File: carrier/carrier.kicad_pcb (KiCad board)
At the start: 2 copper layers, 86.4 x 68.6 mm, 96 parts, among them J1 Conn_01x14, J10 Conn_02x06_Odd_Even, J2 Conn_01x14, J3 Conn_01x14, J4 Conn_01x14, J5 Conn_02x14_Odd_Even, J6 Conn_02x14_Odd_Even, J7 Conn_02x14_Odd_Even, J8 Conn_02x14_Odd_Even, J9 Conn_02x06_Odd_Even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

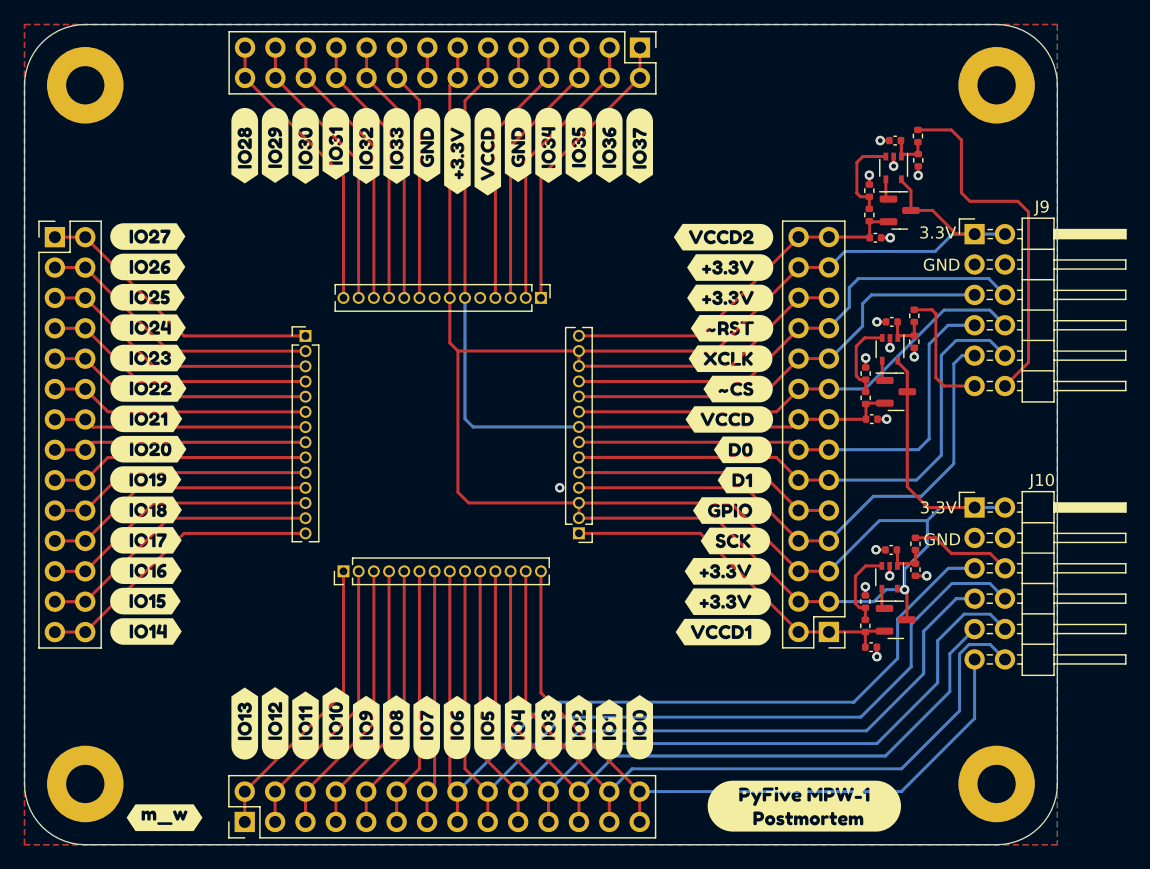
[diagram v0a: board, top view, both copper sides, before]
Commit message: Tweaks based on tnt's feedback
Wired GPIO to PMOD1
Switch 6 IOs on PMOD to attach to a header
Add GND test point
Add alignment holes for breakout
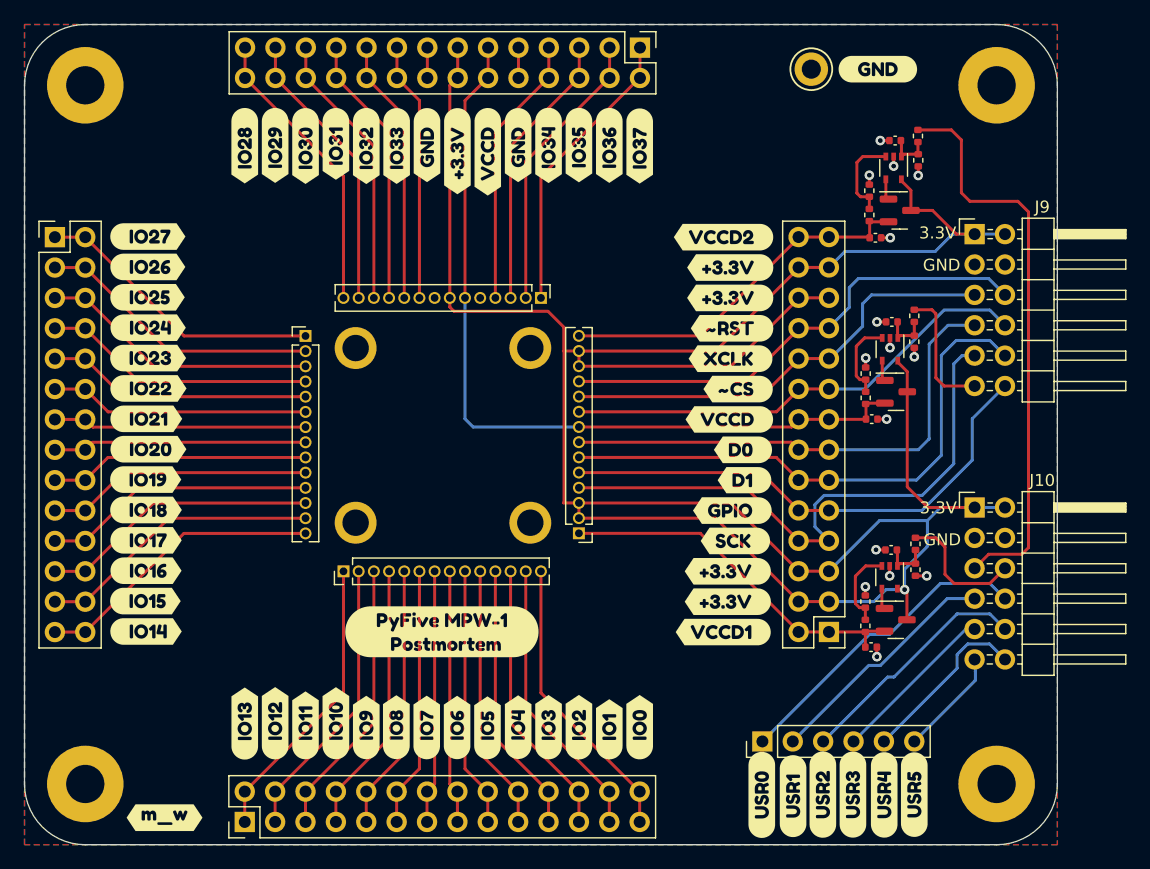
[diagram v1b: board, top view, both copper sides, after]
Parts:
- added ?: , , F.Cu at (162.3, 95.0)
- added ?: , , F.Cu at (176.9, 95.0)
- added ?: , , F.Cu at (176.9, 80.4)
- added ?: , , F.Cu at (162.3, 80.4)
- added J11: Conn_01x06, Connector_PinHeader_2.54mm:PinHeader_1x06_P2.54mm_Vertical, F.Cu at (196.3, 113.3)
- added TP1: TestPoint, TestPoint:TestPoint_Keystone_5005-5009_Compact, F.Cu at (200.4, 57.1)
- added kibuzzard-61D400CC: G***, kibuzzard-61D400CC, F.Cu at (196.3, 117.8)
- added kibuzzard-61D4010F: G***, kibuzzard-61D4010F, F.Cu at (198.9, 117.9)
- added kibuzzard-61D40135: G***, kibuzzard-61D40135, F.Cu at (201.4, 117.7)
- added kibuzzard-61D4014A: G***, kibuzzard-61D4014A, F.Cu at (203.9, 117.7)
- added kibuzzard-61D401EF: G***, kibuzzard-61D401EF, F.Cu at (206.5, 117.8)
- added kibuzzard-61D401FF: G***, kibuzzard-61D401FF, F.Cu at (209.0, 117.7)
- added kibuzzard-61D40313: G***, kibuzzard-61D40313, F.Cu at (206.0, 57.1)
- moved kibuzzard-61D3CE10 33.6 mm to (169.5, 104.1)
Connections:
- J10 pad 10: /IO3 -> /USR2
- J10 pad 11: /IO0 -> /USR5
- J10 pad 12: /IO1 -> /USR4
- J10 pad 5: /IO6 -> /VCCD2_PDM
- J10 pad 7: /IO4 -> /USR1
- J10 pad 8: /IO5 -> /USR0
- J10 pad 9: /IO2 -> /USR3
- J9 pad 12: /VCCD2_PDM -> /GPIO
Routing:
- net /IO5: track 74.8 -> 21.7 mm
- net /IO6: track 74.1 -> 21.2 mm
- net /IO4: track 69.2 -> 22.3 mm
- net /IO3: track 69.7 -> 22.8 mm
- net /IO1: track 65.3 -> 23.8 mm
- net /IO2: track 63.9 -> 23.3 mm
- net /IO0: track 59.8 -> 24.4 mm
- net /USR0: track 0.00 -> 26.3 mm
- net /GPIO: track 22.3 -> 43.3 mm
- net /USR1: track 0.00 -> 20.1 mm
- net /USR2: track 0.00 -> 20.1 mm
- net /VCCD2_PDM: track 30.0 -> 48.0 mm
- net /USR4: track 0.00 -> 14.7 mm
- net /USR3: track 0.00 -> 14.0 mm
- net /USR5: track 0.00 -> 9.00 mm
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
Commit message: carrier: Flexy pin version
Signed-off-by: Sylvain Munaut <tnt@246tNt.com>
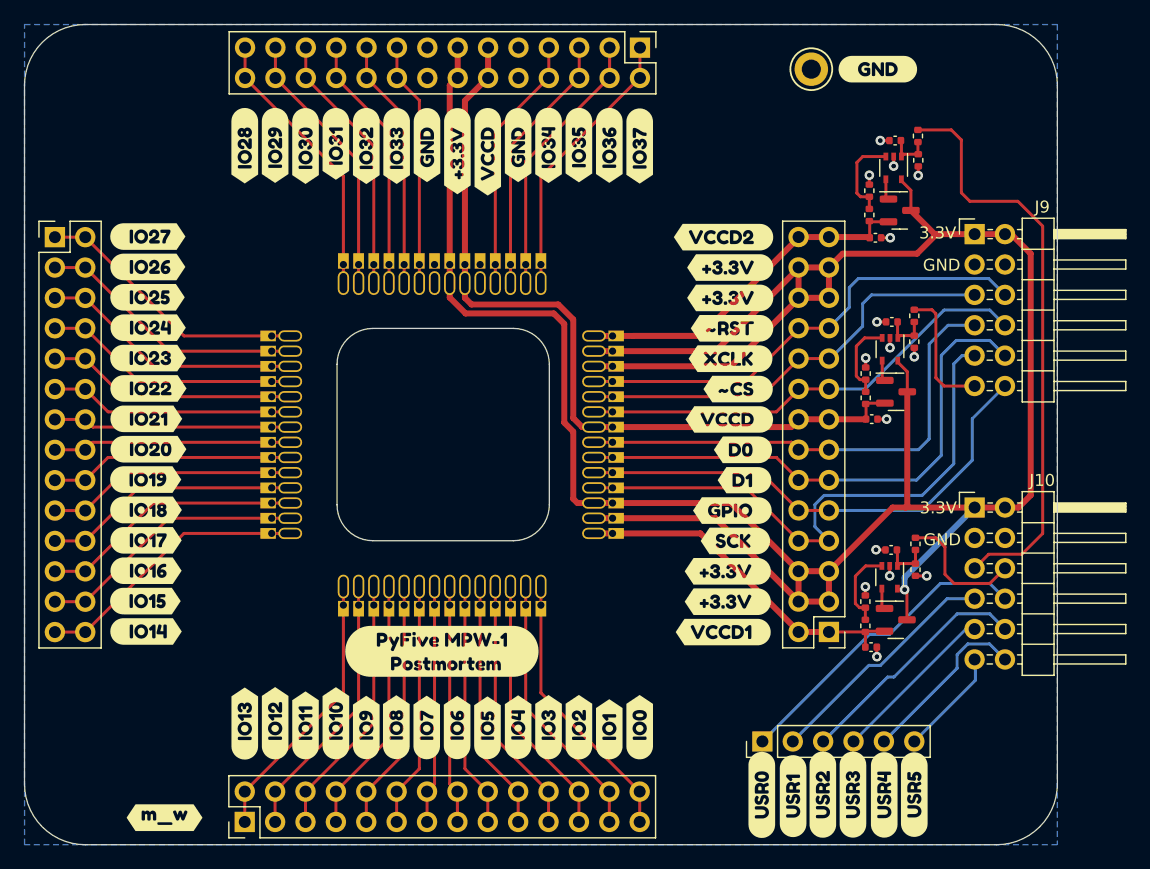
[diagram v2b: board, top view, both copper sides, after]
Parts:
- removed ? (x7): , 
- removed J1, J2, J3, J4: Conn_01x14, Connector_PinHeader_1.27mm:PinHeader_1x14_P1.27mm_Vertical
- removed REF**: MountingHole_3.2mm_M3_Pad, MountingHole:MountingHole_3.2mm_M3_Pad
- added U4: caravel_breakout, Caravel_Board:caravel_breakout_flexy, B.Cu at (169.5, 87.6)
- moved kibuzzard-61D3CE10 1.64 mm to (169.5, 105.8)
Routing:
- net +3V3: track 222.0 -> 237.6 mm
- net GND: track 17.0 -> 11.9 mm
- net /VCCD2: track 30.8 -> 29.5 mm
- net /GPIO: track 43.3 -> 42.0 mm
- net /IO27: track 24.4 -> 23.1 mm
- net /IO26: track 23.9 -> 22.6 mm
- net /IO25: track 23.3 -> 22.0 mm
- net /IO24: track 22.8 -> 21.5 mm
- net /IO23: track 22.3 -> 21.0 mm
- net /IO22: track 21.7 -> 20.5 mm
- net /IO21: track 21.2 -> 19.9 mm
- net /IO20: track 21.2 -> 19.9 mm
- net /IO19: track 21.7 -> 20.5 mm
- net /IO18: track 22.3 -> 21.0 mm
- net /IO17: track 22.8 -> 21.5 mm
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- removed copper zone on F.Cu, net GND
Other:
- outline, holes or cut-outs redrawn
